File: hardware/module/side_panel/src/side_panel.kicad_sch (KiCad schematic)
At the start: 43 parts, among them J1 Top Connector, J2 Bottom Connecor, J3 Conn_01x05, J7 Conn_01x09, M1 GA12-N20 12V 100rpm, Q1 AP2302B, U1 QRE1113GR, U2 QRE1113GR, U3 QRE1113GR, U4 QRE1113GR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

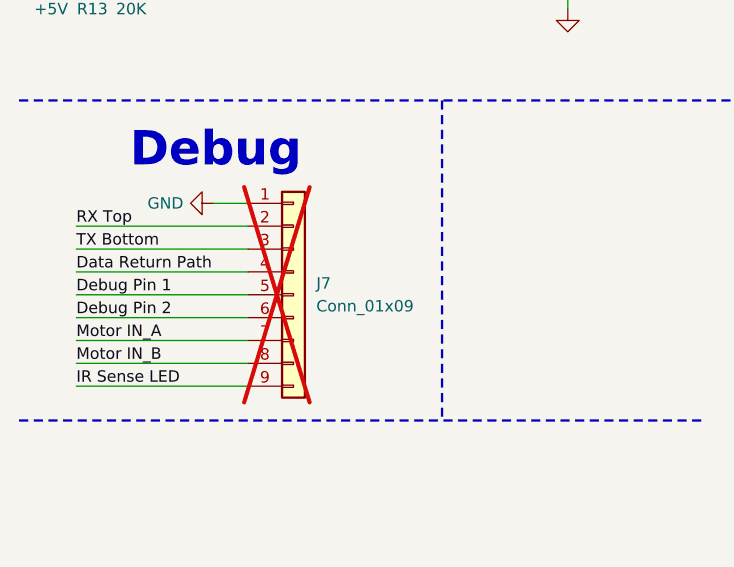
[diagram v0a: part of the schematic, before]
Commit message: Use kibot on sidepanel and top connector
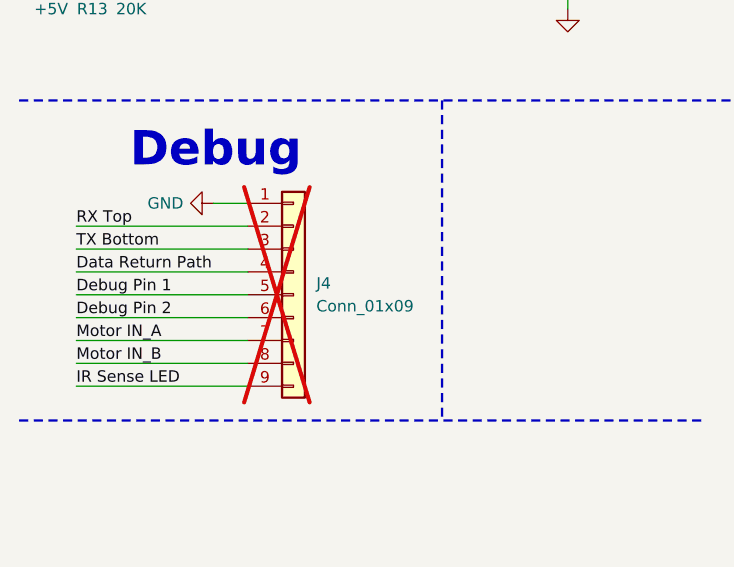
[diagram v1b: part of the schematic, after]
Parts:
- renumbered J7 to J4
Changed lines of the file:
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@@
 	(title_block
 		(title "Side Panel")
-		(date "2024-07-28")
+		(date "${DATE}")
 		(rev "4.0.0")
 		(company "OpenFlap")
-		(comment 1 "Designer: Toon Van Eyck")
+		(comment 1 "${GIT_TAG}")
+		(comment 2 "Repo: github.com/ToonVanEyck/OpenFlap")
+		(comment 3 "Designer: Toon Van Eyck")
 	)
 	(junction
@@
 		(dnp yes)
 		(fields_autoplaced yes)
-		(property "Reference" "J7"
+		(property "Reference" "J4"
 			(at 45.72 237.49 0)
 			(effects
@@
 			(project ""
 				(path "/36bb1b3b-7b5b-4a4c-b4db-cfb27ceb38a1"
-					(reference "J7")
+					(reference "J4")
 					(unit 1)
 				)

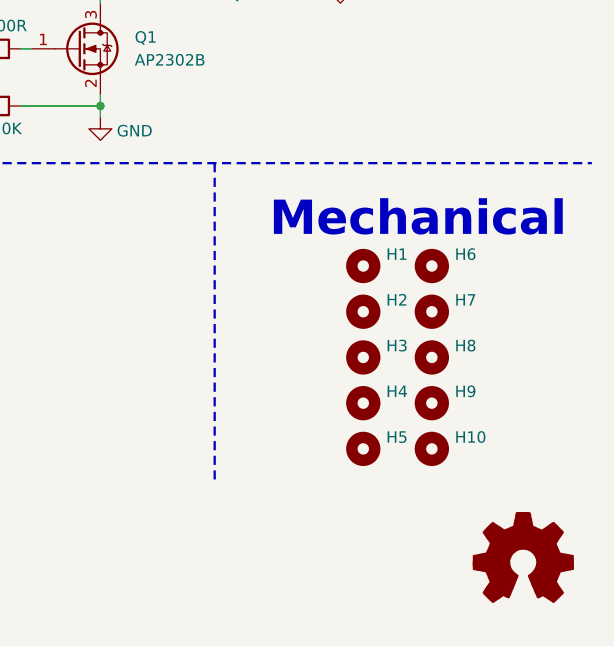
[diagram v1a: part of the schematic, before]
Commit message: Add FreeCad model and update board layout.
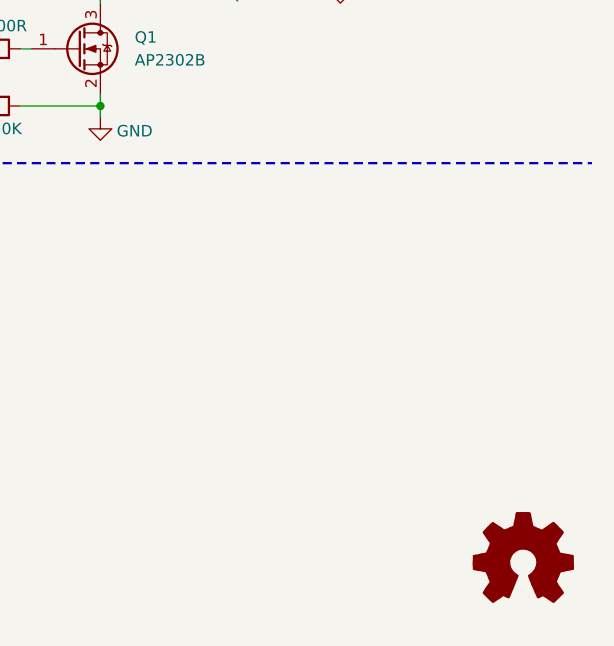
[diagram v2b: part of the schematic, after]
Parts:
- removed H1, H10, H2, H3, H4, H5, H6, H7, H8, H9: MountingHole, MountingHole:MountingHole_2.7mm_M2.5_ISO14580, symbol Mechanical:MountingHole
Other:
- note removed: "Mechanical"

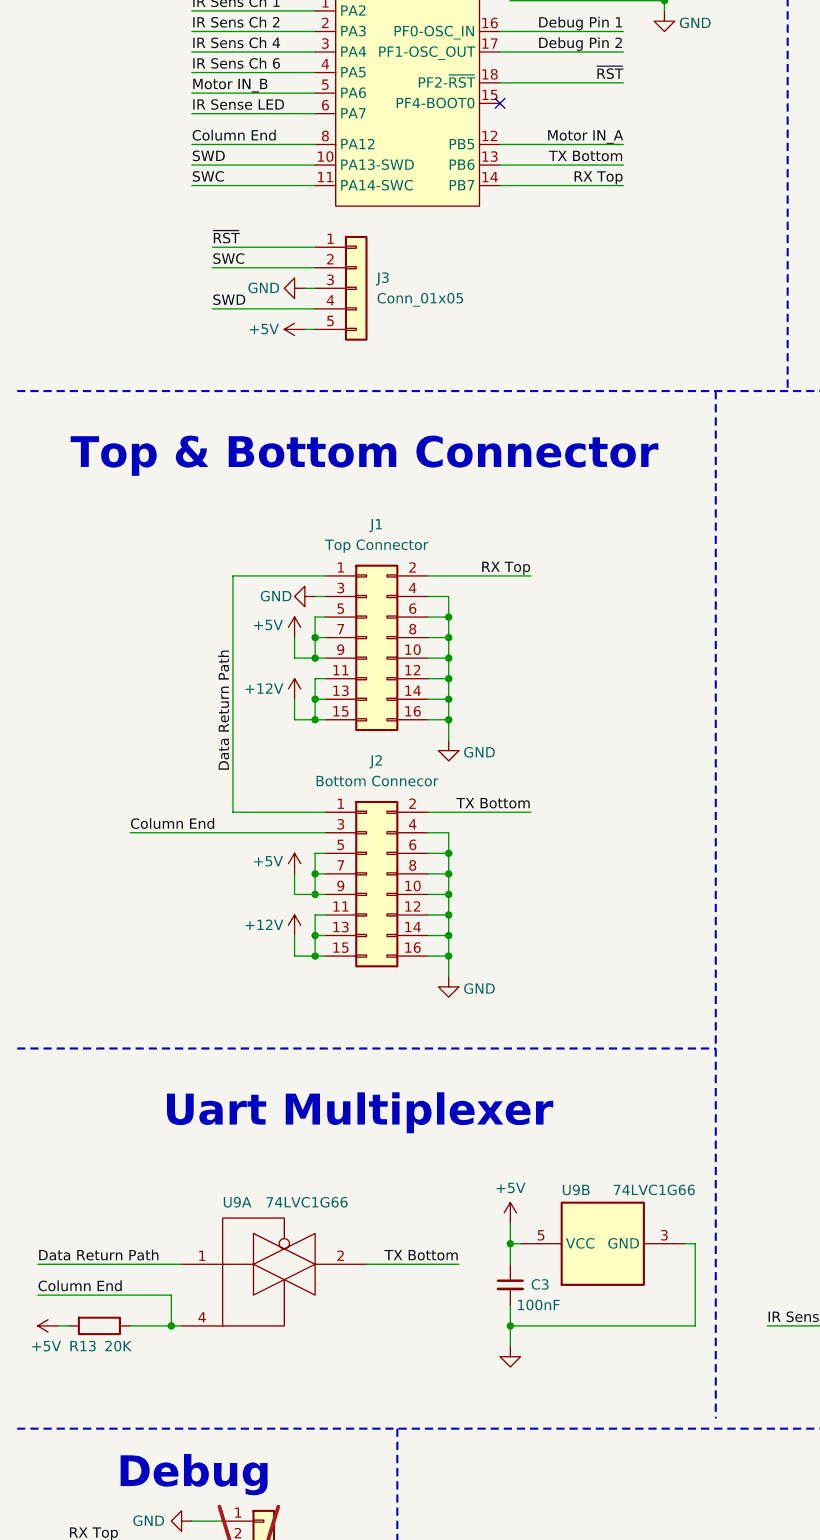
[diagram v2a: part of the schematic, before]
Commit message: Added TVS diode to UART line on side pannel
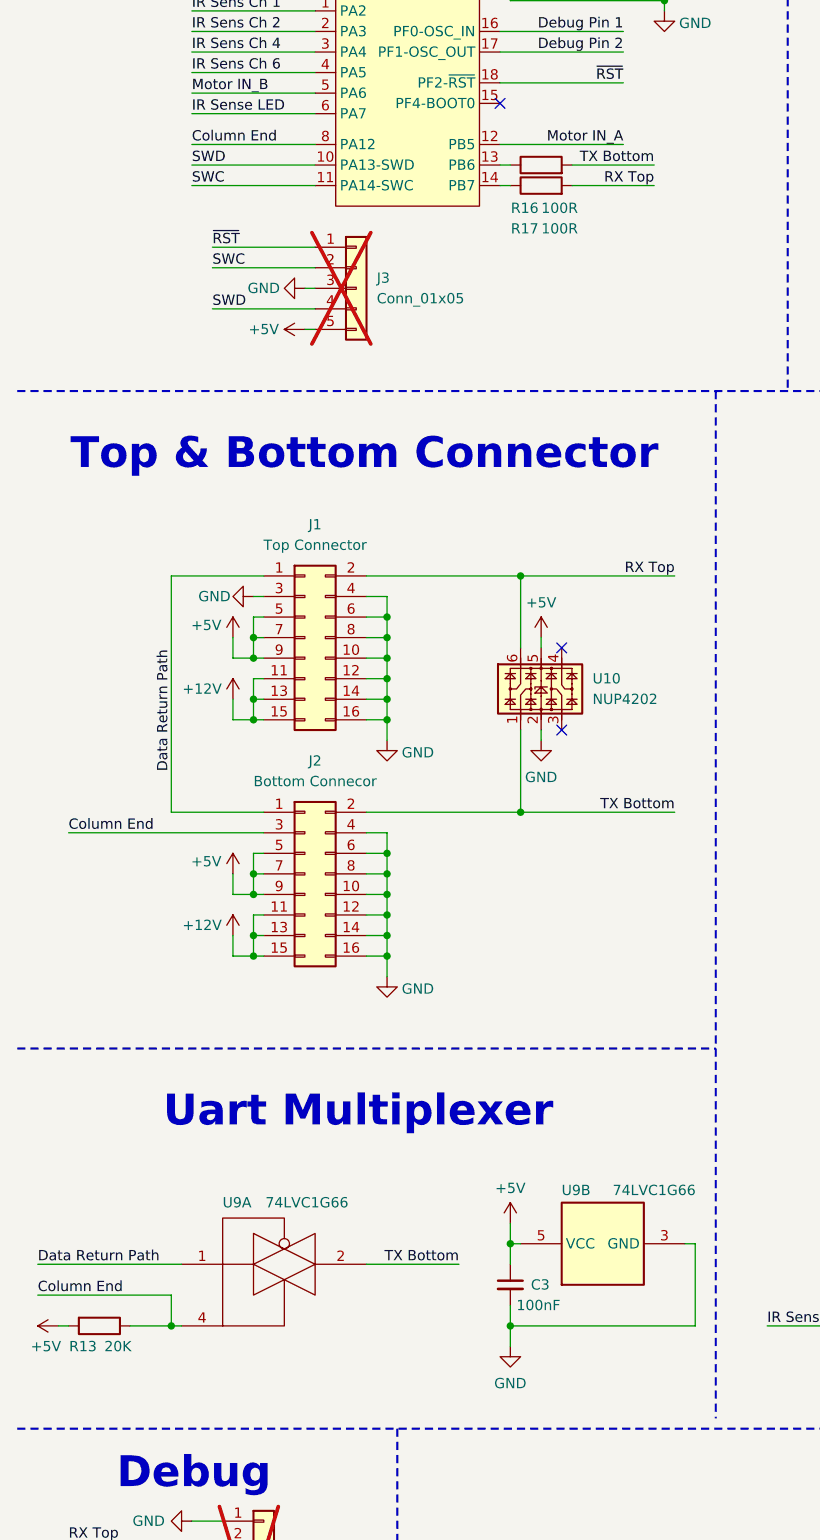
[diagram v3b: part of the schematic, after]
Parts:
- added R16, R17: 100R, Resistor_SMD:R_0805_2012Metric, symbol Device:R
- added U10: NUP4202, Package_TO_SOT_SMD:SOT-363_SC-70-6, symbol Power_Protection:NUP4202
- J3: now not fitted
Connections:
- net +5V: now also U10.5
- net GND: now also U10.2
- net RX Top: now also R17.2, U10.6; no longer U7.14 (PB7)
- net TX Bottom: now also R16.2, U10.1; no longer U7.13 (PB6)
- new net: R17.1, U7.14 (PB7)
- new net: R16.1, U7.13 (PB6)
- no-connect marks 1 -> 3
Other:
- moved on the sheet: J1, J2

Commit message: Added some testpads
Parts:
- U10: footprint Package_TO_SOT_SMD:SOT-363_SC-70-6 -> Package_TO_SOT_SMD:SOT-23-6
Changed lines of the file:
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@@
 			)
 		)
-		(property "Footprint" "Package_TO_SOT_SMD:SOT-363_SC-70-6"
+		(property "Footprint" "Package_TO_SOT_SMD:SOT-23-6"
 			(at 78.74 123.825 0)
 			(effects

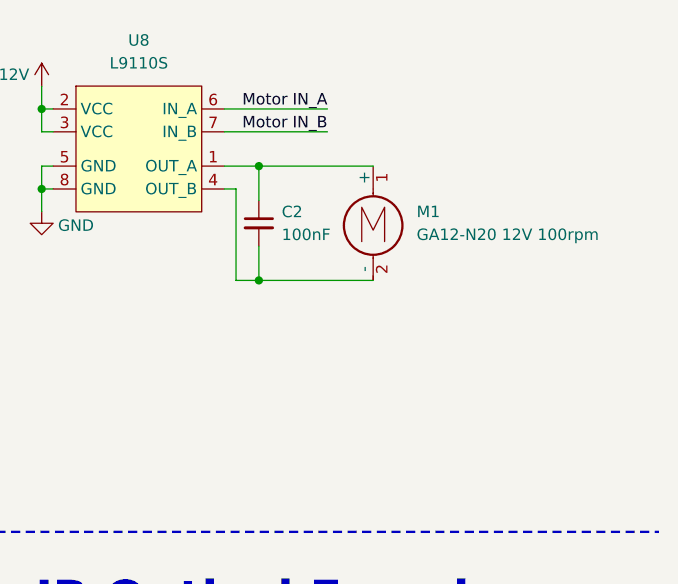
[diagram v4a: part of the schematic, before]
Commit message: reverse motor polarity on side pannel
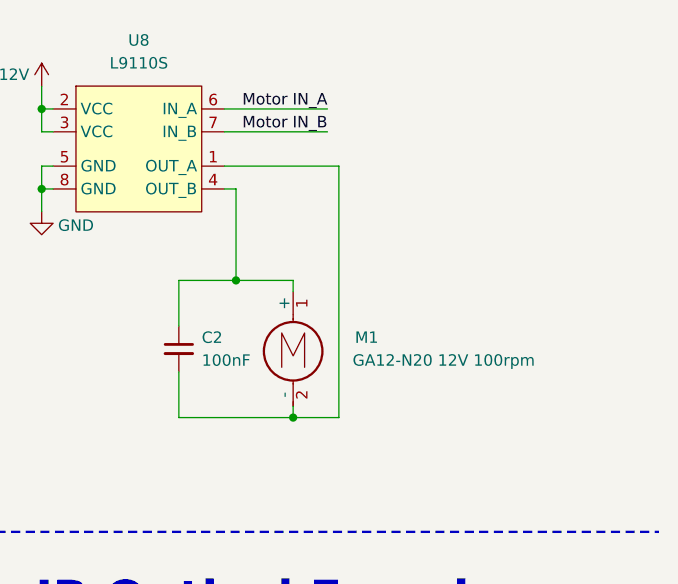
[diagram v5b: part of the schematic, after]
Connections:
- net at C2.1, M1.1 (+): now also U8.4 (OUT_B); no longer U8.1 (OUT_A)
- net at C2.2, M1.2 (-): now also U8.1 (OUT_A); no longer U8.4 (OUT_B)
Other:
- moved on the sheet: C2, M1
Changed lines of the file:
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@@
 		(title "Side Panel")
 		(date "${DATE}")
-		(rev "4.1.0")
+		(rev "4.1.1")
 		(company "OpenFlap")
 		(comment 1 "${GIT_TAG}")
@@
 	)
 	(junction
-		(at 152.4 60.96)
-		(diameter 0)
-		(color 0 0 0 0)
-	)
-	(junction
 		(at 58.42 119.38)
 		(diameter 0)
@@
 	)
 	(junction
-		(at 152.4 48.26)
-		(diameter 0)
-		(color 0 0 0 0)
-	)
-	(junction
 		(at 58.42 156.21)
 		(diameter 0)
@@
 	)
 	(junction
+		(at 156.21 76.2)
+		(diameter 0)
+		(color 0 0 0 0)
+	)
+	(junction
 		(at 31.75 204.47)
 		(diameter 0)
@@
 	)
 	(junction
+		(at 149.86 60.96)
+		(diameter 0)
+		(color 0 0 0 0)
+	)
+	(junction
 		(at 41.91 121.92)
 		(diameter 0)
@@
 	(wire
 		(pts
-			(xy 152.4 48.26) (xy 165.1 48.26)
+			(xy 152.4 157.48) (xy 149.86 157.48)
 		)
 		(stroke
@@
 	(wire
 		(pts
-			(xy 152.4 157.48) (xy 149.86 157.48)
+			(xy 156.21 62.23) (xy 156.21 60.96)
 		)
 		(stroke
@@
 	(wire
 		(pts
-			(xy 152.4 60.96) (xy 149.86 60.96)
-		)
-		(stroke
-			(width 0)
-			(type default)
-		)
-	)
-	(wire
-		(pts
 			(xy 128.27 48.26) (xy 128.27 50.8)
 		)
@@
 	(wire
 		(pts
+			(xy 161.29 76.2) (xy 156.21 76.2)
+		)
+		(stroke
+			(width 0)
+			(type default)
+		)
+	)
+	(wire
+		(pts
 			(xy 124.46 210.82) (xy 124.46 204.47)
 		)
@@
 	(wire
 		(pts
+			(xy 161.29 48.26) (xy 161.29 76.2)
+		)
+		(stroke
+			(width 0)
+			(type default)
+		)
+	)
+	(wire
+		(pts
 			(xy 152.4 190.5) (xy 149.86 190.5)
 		)
@@
 	(wire
 		(pts
+			(xy 143.51 60.96) (xy 149.86 60.96)
+		)
+		(stroke
+			(width 0)
+			(type default)
+		)
+	)
+	(wire
+		(pts
 			(xy 36.83 78.74) (xy 49.53 78.74)
 		)
@@
 	(wire
 		(pts
+			(xy 156.21 76.2) (xy 156.21 74.93)
+		)
+		(stroke
+			(width 0)
+			(type default)
+		)
+	)
+	(wire
+		(pts
 			(xy 58.42 148.59) (xy 58.42 151.13)
 		)
@@
 	(wire
 		(pts
+			(xy 156.21 60.96) (xy 149.86 60.96)
+		)
+		(stroke
+			(width 0)
+			(type default)
+		)
+	)
+	(wire
+		(pts
 			(xy 73.66 40.64) (xy 92.71 40.64)
 		)
@@
 	(wire
 		(pts
-			(xy 148.59 48.26) (xy 152.4 48.26)
+			(xy 148.59 48.26) (xy 161.29 48.26)
 		)
 		(stroke
@@
 	(wire
 		(pts
-			(xy 165.1 60.96) (xy 152.4 60.96)
-		)
-		(stroke
-			(width 0)
-			(type default)
-		)
-	)
-	(wire
-		(pts
 			(xy 43.18 140.97) (xy 31.75 140.97)
 		)
@@
 	(wire
 		(pts
-			(xy 19.05 248.92) (xy 38.1 248.92)
+			(xy 143.51 71.12) (xy 143.51 76.2)
 		)
 		(stroke
@@
 	(wire
 		(pts
-			(xy 39.37 156.21) (xy 39.37 158.75)
+			(xy 19.05 248.92) (xy 38.1 248.92)
 		)
 		(stroke
@@
 	(wire
 		(pts
-			(xy 72.39 60.96) (xy 73.66 60.96)
+			(xy 39.37 156.21) (xy 39.37 158.75)
 		)
 		(stroke
@@
 	(wire
 		(pts
-			(xy 149.86 168.91) (xy 149.86 170.18)
+			(xy 72.39 60.96) (xy 73.66 60.96)
 		)
 		(stroke
@@
 	(wire
 		(pts
-			(xy 156.21 153.67) (xy 149.86 153.67)
+			(xy 149.86 168.91) (xy 149.86 170.18)
 		)
 		(stroke
@@
 	(wire
 		(pts
-			(xy 149.86 50.8) (xy 148.59 50.8)
+			(xy 156.21 153.67) (xy 149.86 153.67)
 		)
 		(stroke
@@
 	(wire
 		(pts
-			(xy 55.88 151.13) (xy 58.42 151.13)
+			(xy 149.86 50.8) (xy 148.59 50.8)
 		)
 		(stroke
@@
 	(wire
 		(pts
-			(xy 152.4 57.15) (xy 152.4 60.96)
+			(xy 55.88 151.13) (xy 58.42 151.13)
 		)
 		(stroke
@@
 	(wire
 		(pts
+			(xy 143.51 76.2) (xy 156.21 76.2)
+		)
+		(stroke
+			(width 0)
+			(type default)
+		)
+	)
+	(wire
+		(pts
 			(xy 133.35 204.47) (xy 134.62 204.47)
 		)
@@
 	(wire
 		(pts
+			(xy 143.51 66.04) (xy 143.51 60.96)
+		)
+		(stroke
+			(width 0)
+			(type default)
+		)
+	)
+	(wire
+		(pts
 			(xy 58.42 124.46) (xy 58.42 127)
 		)
@@
 	(wire
 		(pts
-			(xy 152.4 48.26) (xy 152.4 52.07)
-		)
-		(stroke
-			(width 0)
-			(type default)
-		)
-	)
-	(wire
-		(pts
 			(xy 15.24 200.66) (xy 31.75 200.66)
 		)
@@
 	(symbol
 		(lib_id "Motor:Motor_DC")
-		(at 165.1 53.34 0)
+		(at 156.21 67.31 0)
 		(unit 1)
 		(exclude_from_sim no)
@@
 		(dnp no)
 		(property "Reference" "M1"
-			(at 169.926 53.34 0)
+			(at 163.068 67.31 0)
 			(effects
 				(font
@@
 		)
 		(property "Value" "GA12-N20 12V 100rpm"
-			(at 169.926 55.88 0)
+			(at 162.814 69.85 0)
 			(effects
 				(font
@@
 		)
 		(property "Footprint" "GA12-N20:GA12-N20 Motor Vertical"
-			(at 165.1 55.626 0)
+			(at 156.21 69.596 0)
 			(effects
 				(font
@@
 		)
 		(property "Datasheet" "~"
-			(at 165.1 55.626 0)
+			(at 156.21 69.596 0)
 			(effects
 				(font
@@
 		)
 		(property "Description" "DC Motor"
-			(at 165.1 53.34 0)
+			(at 156.21 67.31 0)
 			(effects
 				(font
@@
 	(symbol
 		(lib_id "Device:C_Small")
-		(at 152.4 54.61 0)
+		(at 143.51 68.58 0)
 		(unit 1)
 		(exclude_from_sim no)
@@
 		(dnp no)
 		(property "Reference" "C2"
-			(at 154.94 53.3463 0)
+			(at 146.05 67.3163 0)
 			(effects
 				(font
@@
 		)
 		(property "Value" "100nF"
-			(at 154.94 55.8863 0)
+			(at 146.05 69.8563 0)
 			(effects
 				(font
@@
 		)
 		(property "Footprint" "Capacitor_SMD:C_0805_2012Metric"
-			(at 152.4 54.61 0)
+			(at 143.51 68.58 0)
 			(effects
 				(font
@@
 		)
 		(property "Datasheet" "~"
-			(at 152.4 54.61 0)
+			(at 143.51 68.58 0)
 			(effects
 				(font
@@
 		)
 		(property "Description" "Unpolarized capacitor, small symbol"
-			(at 152.4 54.61 0)
+			(at 143.51 68.58 0)
 			(effects
 				(font

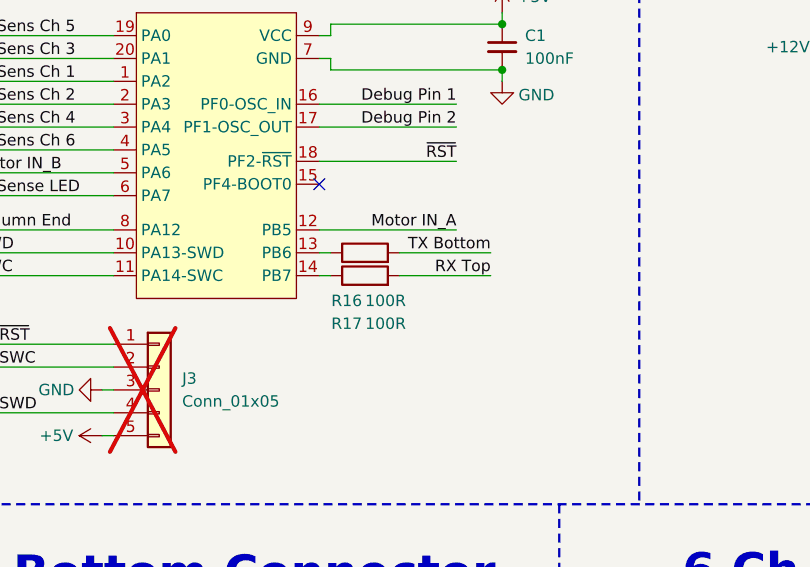
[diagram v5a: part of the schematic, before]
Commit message: remove series resistors from uart lines on modules
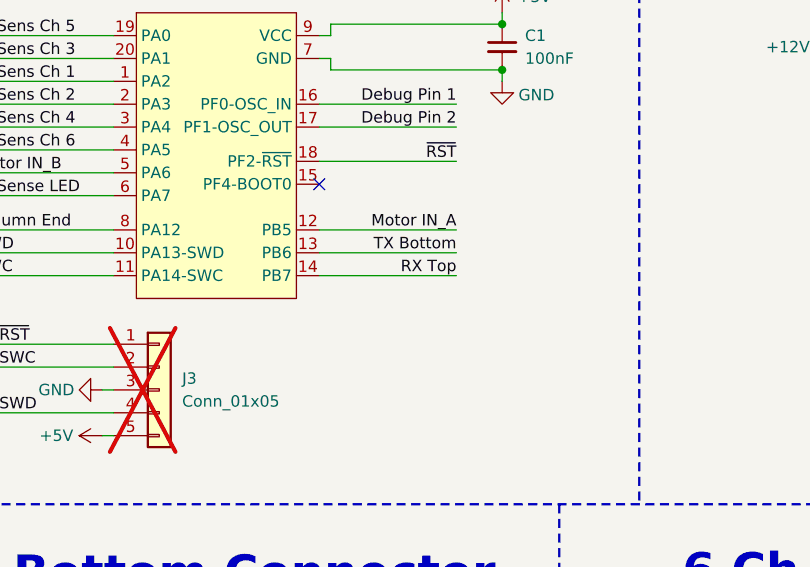
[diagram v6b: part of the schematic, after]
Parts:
- removed R16, R17: 100R, Resistor_SMD:R_0805_2012Metric, symbol Device:R
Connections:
- net RX Top: now also U7.14 (PB7)
- net TX Bottom: now also U7.13 (PB6)
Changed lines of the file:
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@@
 		(title "Side Panel")
 		(date "${DATE}")
-		(rev "4.1.1")
+		(rev "4.1.2")
 		(company "OpenFlap")
 		(comment 1 "${GIT_TAG}")
@@
 	(wire
 		(pts
-			(xy 72.39 63.5) (xy 73.66 63.5)
+			(xy 72.39 63.5) (xy 87.63 63.5)
 		)
 		(stroke
@@
 	(wire
 		(pts
-			(xy 81.28 60.96) (xy 91.44 60.96)
-		)
-		(stroke
-			(width 0)
-			(type default)
-		)
-	)
-	(wire
-		(pts
 			(xy 149.86 60.96) (xy 149.86 50.8)
 		)
@@
 	(wire
 		(pts
-			(xy 81.28 63.5) (xy 91.44 63.5)
-		)
-		(stroke
-			(width 0)
-			(type default)
-		)
-	)
-	(wire
-		(pts
 			(xy 168.91 113.03) (xy 168.91 114.3)
 		)
@@
 	(wire
 		(pts
-			(xy 72.39 60.96) (xy 73.66 60.96)
+			(xy 72.39 60.96) (xy 87.63 60.96)
 		)
 		(stroke
@@
 	)
 	(label "TX Bottom"
-		(at 91.44 60.96 180)
+		(at 87.63 60.96 180)
 		(fields_autoplaced yes)
 		(effects
@@
 	)
 	(label "RX Top"
-		(at 91.44 63.5 180)
+		(at 87.63 63.5 180)
 		(fields_autoplaced yes)
 		(effects
@@
 	)
 	(symbol
-		(lib_id "Device:R")
-		(at 77.47 63.5 90)
-		(unit 1)
-		(exclude_from_sim no)
-		(in_bom yes)
-		(on_board yes)
-		(dnp no)
-		(property "Reference" "R17"
-			(at 75.438 68.834 90)
-			(effects
-				(font
-					(size 1.27 1.27)
-				)
-			)
-		)
-		(property "Value" "100R"
-			(at 79.756 68.834 90)
-			(effects
-				(font
-					(size 1.27 1.27)
-				)
-			)
-		)
-		(property "Footprint" "Resistor_SMD:R_0805_2012Metric"
-			(at 77.47 65.278 90)
-			(effects
-				(font
-					(size 1.27 1.27)
-				)
-				(hide yes)
-			)
-		)
-		(property "Datasheet" "~"
-			(at 77.47 63.5 0)
-			(effects
-				(font
-					(size 1.27 1.27)
-				)
-				(hide yes)
-			)
-		)
-		(property "Description" "Resistor"
-			(at 77.47 63.5 0)
-			(effects
-				(font
-					(size 1.27 1.27)
-				)
-				(hide yes)
-			)
-		)
-		(pin "1"
-		)
-		(pin "2"
-		)
-		(instances
-			(project "side_panel"
-				(path "/36bb1b3b-7b5b-4a4c-b4db-cfb27ceb38a1"
-					(reference "R17")
-					(unit 1)
-				)
-			)
-		)
-	)
-	(symbol
 		(lib_id "power:+5V")
 		(at 39.37 119.38 0)
@@
 					(unit 1)
 				)
-			)
-		)
-	)
-	(symbol
-		(lib_id "Device:R")
-		(at 77.47 60.96 90)
-		(unit 1)
-		(exclude_from_sim no)
-		(in_bom yes)
-		(on_board yes)
-		(dnp no)
-		(property "Reference" "R16"
-			(at 75.438 66.294 90)
-			(effects
-				(font
-					(size 1.27 1.27)
-				)
-			)
-		)
-		(property "Value" "100R"
-			(at 79.756 66.294 90)
-			(effects
-				(font
-					(size 1.27 1.27)
-				)
-			)
-		)
-		(property "Footprint" "Resistor_SMD:R_0805_2012Metric"
-			(at 77.47 62.738 90)
-			(effects
-				(font
-					(size 1.27 1.27)
-				)
-				(hide yes)
-			)
-		)
-		(property "Datasheet" "~"
-			(at 77.47 60.96 0)
-			(effects
-				(font
-					(size 1.27 1.27)
-				)
-				(hide yes)
-			)
-		)
-		(property "Description" "Resistor"
-			(at 77.47 60.96 0)
-			(effects
-				(font
-					(size 1.27 1.27)
-				)
-				(hide yes)
-			)
-		)
-		(pin "1"
-		)
-		(pin "2"
-		)
-		(instances
-			(project "side_panel"
-				(path "/36bb1b3b-7b5b-4a4c-b4db-cfb27ceb38a1"
-					(reference "R16")
-					(unit 1)
-				)
